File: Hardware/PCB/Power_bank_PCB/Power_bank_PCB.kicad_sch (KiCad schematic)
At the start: 86 parts, among them IC1 TPS63070RNMR, IC2 TPS63070RNMR, J1 Fotopanel_connector, J2 Vout, J3 Alterative_charging, Q1 8205A, Q2 2N7002, Q3 DMP3099L, U1 TP4056-42-ESOP8, U2 MCP4018-xxxxLT, U3 DW01A, U4 STM32U031F8Px, U5 INA219AxD, U6 TPS61022

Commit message: KiCad schematic: add parts, adjust layout
Update Power_bank_PCB KiCad project and schematic. Changes include: update used_designators; add/position new symbols (C28, C29, R28, R29, Q4 and several power symbols / #PWR entries); add multiple junctions and wires; relabel text (Fotopanel_enable → Fotopanel_disable, add Foto_raw labels); adjust component values/placements (R18 10k→100k, MCP4018 value refined); move USB connector J2 and update related coordinates. Mostly coordinate/layout and net wiring edits to reflect new parts and routing.
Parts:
- added C28, C29: 10u, symbol Device:C
- added Q4: 2N7002, Package_TO_SOT_SMD:SOT-23, symbol Transistor_FET:2N7002
- added R28: 4.7k, symbol Device:R
- added R29: 3k, symbol Device:R
- R18: value 10k -> 100k
- U2: value MCP4018-xxxxLT -> MCP4018-10k
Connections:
- net +3.3V: now also R28.1; no longer R18.2
- net 5V: now also C28.2, C29.2
- net GND: now also C28.1, C29.1, R29.2
- net SCL: now also R16.2, U4.1 (PB8/PB9); no longer R17.2, U4.19 (PB7)
- net SDA: now also R17.2, U4.19 (PB7); no longer R16.2, U4.1 (PB8/PB9)
- net USB_FLAG: now also Q4.1 (G); no longer U4.4 (PC14)
- net Foto_raw: now reaches J1.2 (Pin_2), R20.1, U5.8 (IN+)
- net Foto_raw: now also R18.2
- net at R5.2, U2.6 (A): now also R29.1
- net Fotopanel_enable renamed Fotopanel_disable
- new net: Q4.2 (S), U4.4 (PC14)
- new net: Q4.3 (D), R28.2
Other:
- moved on the sheet: J2

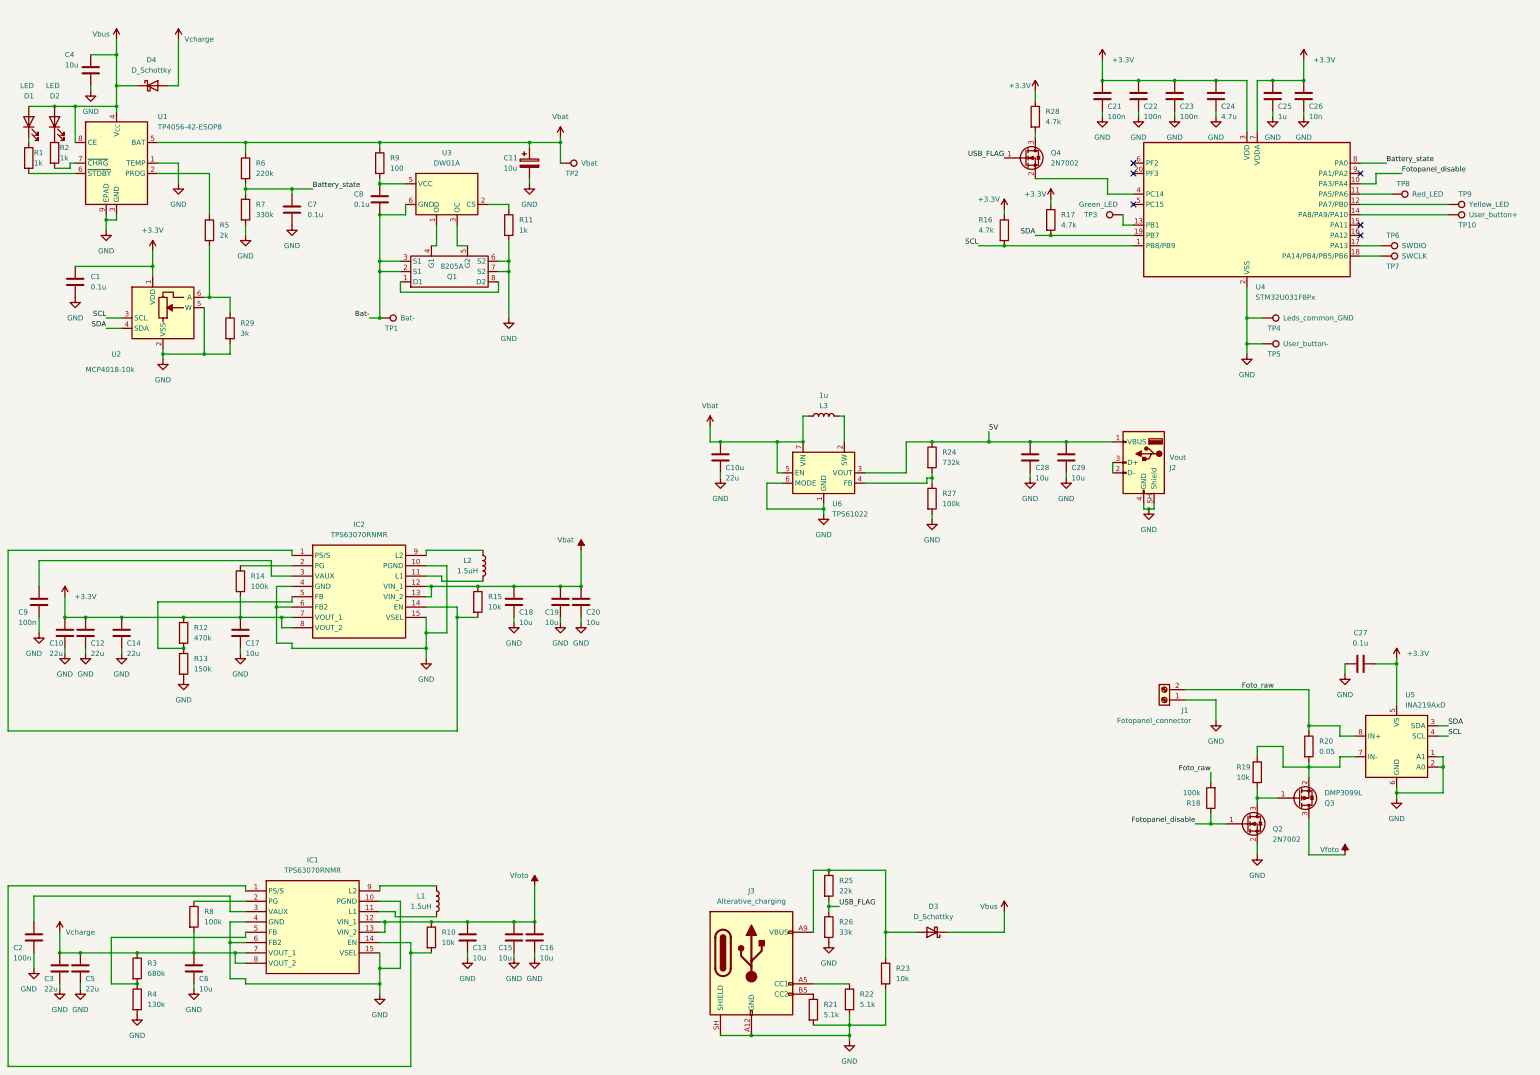
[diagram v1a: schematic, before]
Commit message: Fixed cold-start issue
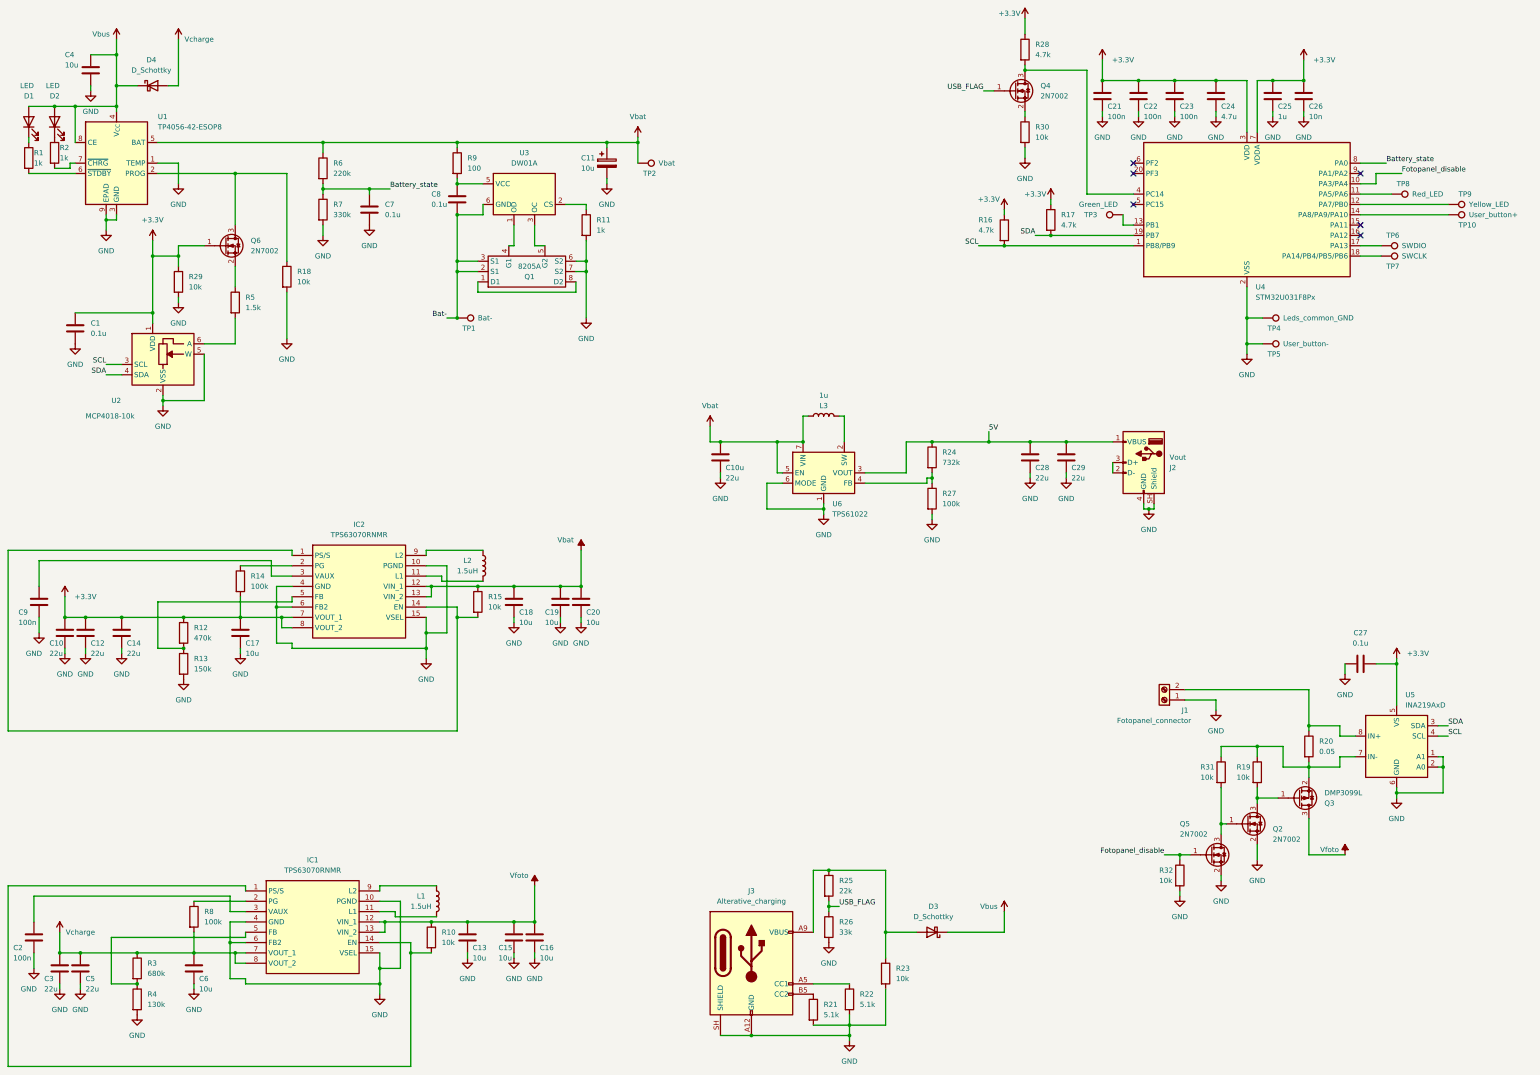
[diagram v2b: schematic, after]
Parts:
- added Q5, Q6: 2N7002, Package_TO_SOT_SMD:SOT-23, symbol Transistor_FET:2N7002
- added R30, R31, R32: 10k, symbol Device:R
- C28, C29: value 10u -> 22u
- R18: value 100k -> 10k
- R29: value 3k -> 10k
- R5: value 2k -> 1.5k
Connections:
- net +3.3V: now also R29.1, Q6.1 (G)
- net Fotopanel_disable: now also Q5.1 (G), R32.1; no longer Q2.1 (G), R18.1
- net GND: now also R18.2, Q5.2 (S), R30.2, R32.2
- net at Q3.2 (S), R19.1, R20.2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: now also R31.1
- net at U1.2 (PROG): now also R18.1, Q6.3 (D); no longer R5.1
- net at R5.2, U2.6 (A): no longer R29.1
- net at Q4.2 (S): now also R30.1; no longer U4.4 (PC14)
- net at Q4.3 (D), R28.2: now also U4.4 (PC14)
- net Foto_raw: no longer names the net of J1.2 (Pin_2), R20.1, U5.8 (IN+)
- net Foto_raw: no longer R18.2
- new net: Q2.1 (G), Q5.3 (D), R31.2
- new net: Q6.2 (S), R5.1
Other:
- moved on the sheet: C1, C11, C7, C8, Q1, Q4, R11, R28, R5, R6, R7, R9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

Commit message: First attempt to do PCB layout
done basic concept without main DC/DC converters
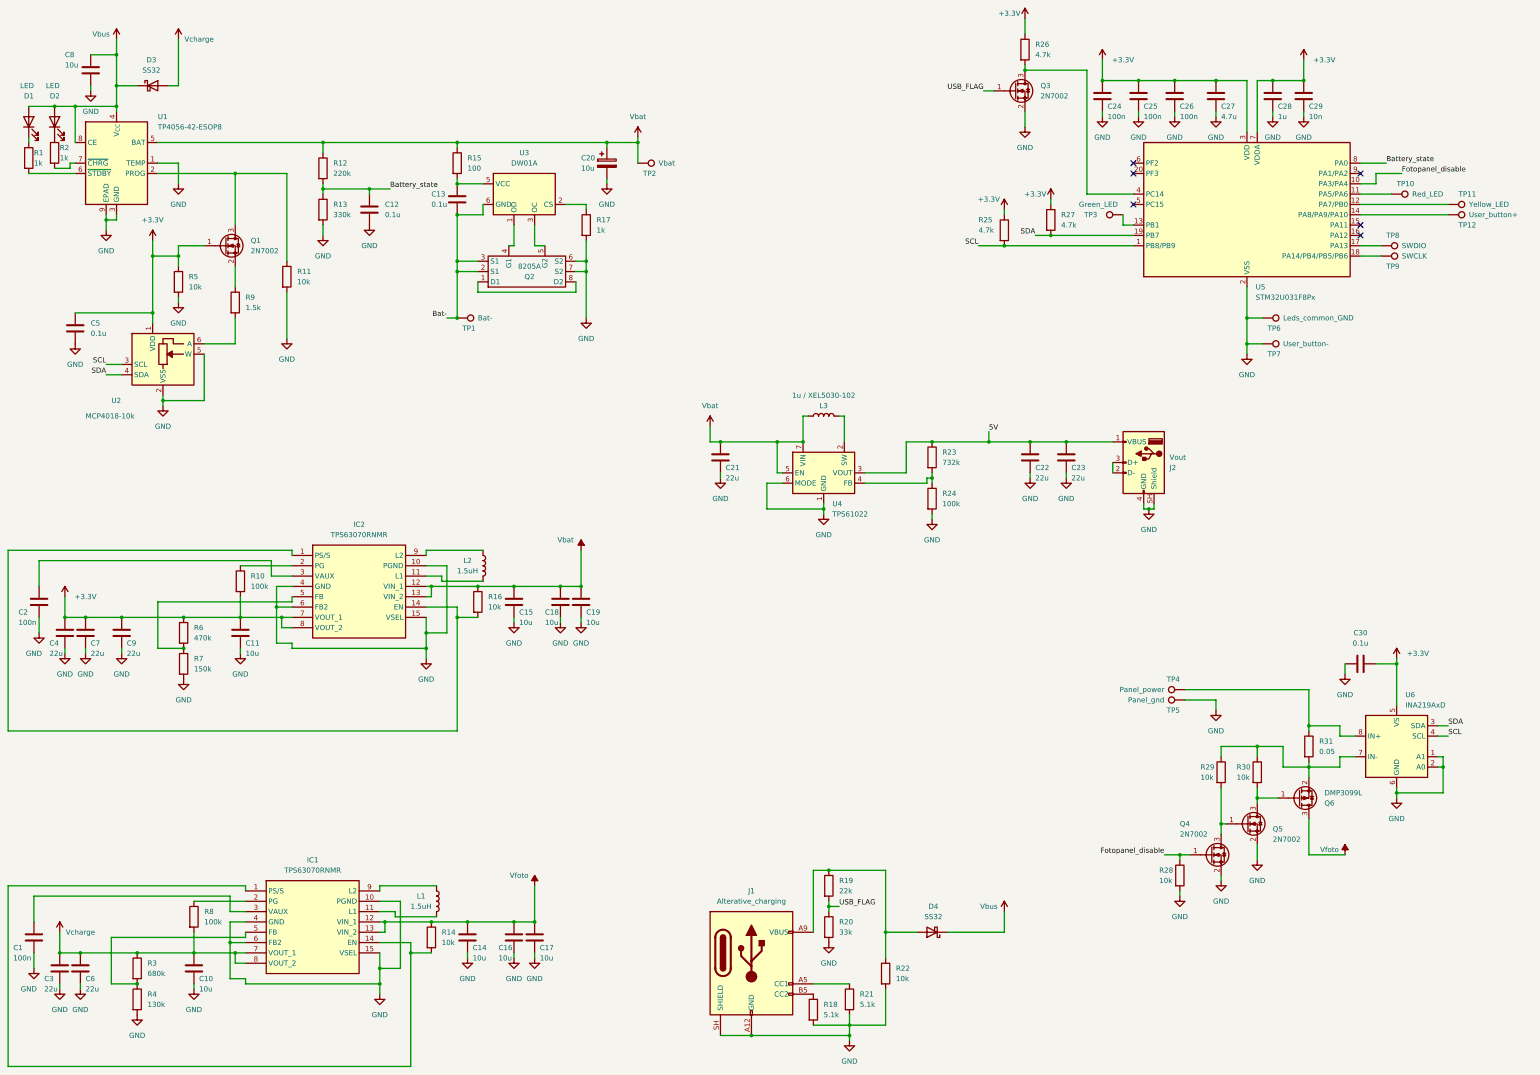
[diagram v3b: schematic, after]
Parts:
- removed D3, D4: D_Schottky, symbol Device:D_Schottky
- removed J1: Fotopanel_connector, symbol Connector:Screw_Terminal_01x02
- removed R30: 10k, symbol Device:R
- added D3, D4: SS32, Diode_SMD:D_SMA, symbol Diode:SS32
- added TP4: Panel_power, TestPoint:TestPoint_Pad_D4.0mm, symbol Connector:TestPoint
- added TP5: Panel_gnd, TestPoint:TestPoint_Pad_D4.0mm, symbol Connector:TestPoint
- C1: renamed from C2; footprint (none) -> Capacitor_SMD:C_1206_3216Metric
- C10: renamed from C6; footprint (none) -> Capacitor_SMD:C_1206_3216Metric
- C11: renamed from C17; footprint (none) -> Capacitor_SMD:C_1206_3216Metric
- C12: renamed from C7; footprint (none) -> Capacitor_SMD:C_1206_3216Metric
- C13: renamed from C8; footprint (none) -> Capacitor_SMD:C_1206_3216Metric
- C14: renamed from C13; footprint (none) -> Capacitor_SMD:C_1206_3216Metric
- C15: renamed from C18; footprint (none) -> Capacitor_SMD:C_1206_3216Metric
- C16: renamed from C15; footprint (none) -> Capacitor_SMD:C_1206_3216Metric
- C17: renamed from C16; footprint (none) -> Capacitor_SMD:C_1206_3216Metric
- C18: renamed from C19; footprint (none) -> Capacitor_SMD:C_1206_3216Metric
- C19: renamed from C20; footprint (none) -> Capacitor_SMD:C_1206_3216Metric
- C2: renamed from C9; footprint (none) -> Capacitor_SMD:C_1206_3216Metric
- C20: renamed from C11; footprint (none) -> Capacitor_SMD:C_1206_3216Metric
- C21: renamed from C10u; footprint (none) -> Capacitor_SMD:C_1206_3216Metric
- C22: renamed from C28; footprint (none) -> Capacitor_SMD:C_1206_3216Metric
- C23: renamed from C29; footprint (none) -> Capacitor_SMD:C_1206_3216Metric
- C24: renamed from C21; footprint (none) -> Capacitor_SMD:C_1206_3216Metric
- C25: renamed from C22; footprint (none) -> Capacitor_SMD:C_1206_3216Metric
- C26: renamed from C23; footprint (none) -> Capacitor_SMD:C_1206_3216Metric
- C27: renamed from C24; footprint (none) -> Capacitor_SMD:C_1206_3216Metric
- C28: renamed from C25; footprint (none) -> Capacitor_SMD:C_1206_3216Metric
- C29: renamed from C26; footprint (none) -> Capacitor_SMD:C_1206_3216Metric
- C3: footprint (none) -> Capacitor_SMD:C_1206_3216Metric
- C30: renamed from C27; footprint (none) -> Capacitor_SMD:C_1206_3216Metric
- C4: renamed from C10; footprint (none) -> Capacitor_SMD:C_1206_3216Metric
- C5: renamed from C1; footprint (none) -> Capacitor_SMD:C_1206_3216Metric
- C6: renamed from C5; footprint (none) -> Capacitor_SMD:C_1206_3216Metric
- C7: renamed from C12; footprint (none) -> Capacitor_SMD:C_1206_3216Metric
- C8: renamed from C4; footprint (none) -> Capacitor_SMD:C_1206_3216Metric
- C9: renamed from C14; footprint (none) -> Capacitor_SMD:C_1206_3216Metric
- D1, D2: footprint (none) -> LED_SMD:LED_1206_3216Metric_Pad1.42x1.75mm_HandSolder
- L3: value 1u -> 1u / XEL5030-102; footprint (none) -> Inductor_SMD:L_Coilcraft_XAL5030-XXX
- R1, R2, R3, R4, R8: footprint (none) -> Resistor_SMD:R_1206_3216Metric
- R10: renamed from R14; footprint (none) -> Resistor_SMD:R_1206_3216Metric
- R11: renamed from R18; footprint (none) -> Resistor_SMD:R_1206_3216Metric
- R12: renamed from R6; footprint (none) -> Resistor_SMD:R_1206_3216Metric
- R13: renamed from R7; footprint (none) -> Resistor_SMD:R_1206_3216Metric
- R14: renamed from R10; footprint (none) -> Resistor_SMD:R_1206_3216Metric
- R15: renamed from R9; footprint (none) -> Resistor_SMD:R_1206_3216Metric
- R16: renamed from R15; footprint (none) -> Resistor_SMD:R_1206_3216Metric
- R17: renamed from R11; footprint (none) -> Resistor_SMD:R_1206_3216Metric
- R18: renamed from R21; footprint (none) -> Resistor_SMD:R_1206_3216Metric
- R19: renamed from R25; footprint (none) -> Resistor_SMD:R_1206_3216Metric
- R20: renamed from R26; footprint (none) -> Resistor_SMD:R_1206_3216Metric
- R21: renamed from R22; footprint (none) -> Resistor_SMD:R_1206_3216Metric
- R22: renamed from R23; footprint (none) -> Resistor_SMD:R_1206_3216Metric
- R23: renamed from R24; footprint (none) -> Resistor_SMD:R_1206_3216Metric
- R24: renamed from R27; footprint (none) -> Resistor_SMD:R_1206_3216Metric
- R25: renamed from R16; footprint (none) -> Resistor_SMD:R_1206_3216Metric
- R26: renamed from R28; footprint (none) -> Resistor_SMD:R_1206_3216Metric
- R27: renamed from R17; footprint (none) -> Resistor_SMD:R_1206_3216Metric
- R28: renamed from R32; footprint (none) -> Resistor_SMD:R_1206_3216Metric
- R29: renamed from R31; footprint (none) -> Resistor_SMD:R_1206_3216Metric
- R30: renamed from R19; footprint (none) -> Resistor_SMD:R_1206_3216Metric
- R31: renamed from R20; footprint (none) -> Resistor_SMD:R_1206_3216Metric
- R5: renamed from R29; footprint (none) -> Resistor_SMD:R_1206_3216Metric
- R6: renamed from R12; footprint (none) -> Resistor_SMD:R_1206_3216Metric
- R7: renamed from R13; footprint (none) -> Resistor_SMD:R_1206_3216Metric
- R9: renamed from R5; footprint (none) -> Resistor_SMD:R_1206_3216Metric
- TP1, TP2, TP3: footprint Connector_Pin:Pin_D1.3mm_L11.0mm_LooseFit -> TestPoint:TestPoint_Pad_D4.0mm
- TP10: renamed from TP8; footprint Connector_Pin:Pin_D1.3mm_L11.0mm_LooseFit -> TestPoint:TestPoint_Pad_D4.0mm
- TP11: renamed from TP9; footprint Connector_Pin:Pin_D1.3mm_L11.0mm_LooseFit -> TestPoint:TestPoint_Pad_D4.0mm
- TP12: renamed from TP10; footprint Connector_Pin:Pin_D1.3mm_L11.0mm_LooseFit -> TestPoint:TestPoint_Pad_D4.0mm
- TP6: renamed from TP4; footprint Connector_Pin:Pin_D1.3mm_L11.0mm_LooseFit -> TestPoint:TestPoint_Pad_D4.0mm
- TP7: renamed from TP5; footprint Connector_Pin:Pin_D1.3mm_L11.0mm_LooseFit -> TestPoint:TestPoint_Pad_D4.0mm
- TP8: renamed from TP6; footprint Connector_Pin:Pin_D1.3mm_L11.0mm_LooseFit -> TestPoint:TestPoint_Pad_D4.0mm
- TP9: renamed from TP7; footprint Connector_Pin:Pin_D1.3mm_L11.0mm_LooseFit -> TestPoint:TestPoint_Pad_D4.0mm
- renumbered J3 to J1, Q6 to Q1, Q1 to Q2, Q4 to Q3, Q5 to Q4, Q2 to Q5, Q3 to Q6, U6 to U4, U4 to U5, U5 to U6
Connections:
- net GND: now also Q3.2 (S), TP5.1
- net Vbus: now also D3.1 (K), D4.1 (K)
- net Vcharge: now also D3.2 (A)
- net at J1.A9 (VBUS), J1.B9 (VBUS), R19.1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: now also D4.2 (A)
- net at R31.1, U6.8 (IN+): now also TP4.1
